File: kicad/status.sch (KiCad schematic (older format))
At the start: 34 parts, among them U28 74HC04, U29 74HC04

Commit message: bugfixed design
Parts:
- renumbered D30 to D52, D31 to D53, D32 to D54, D33 to D55, D34 to D56, D35 to D57, D36 to D58, D37 to D59, D38 to D60, D39 to D61, D40 to D62, D67 to D63, D41 to D64, D42 to D65, D43 to D66, D44 to D67, R7 to R24, R8 to R25, R9 to R26, R10 to R27, R11 to R28, R12 to R29, R13 to R30, R14 to R31, R15 to R32, R16 to R33, R17 to R34, R30 to R35, R18 to R36, R19 to R37, R20 to R38, R21 to R39, U28 to U45, U29 to U46

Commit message: design as built
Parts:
- renumbered D52 to D1101, D53 to D1102, D54 to D1103, D55 to D1104, D56 to D1105, D57 to D1106, D58 to D1107, D59 to D1108, D60 to D1109, D61 to D1110, D62 to D1111, D63 to D1112, D64 to D1113, D65 to D1114, D66 to D1115, D67 to D1116, R24 to R1101, R25 to R1102, R26 to R1103, R27 to R1104, R28 to R1105, R29 to R1106, R30 to R1107, R31 to R1108, R32 to R1109, R33 to R1110, R34 to R1111, R35 to R1112, R36 to R1113, R37 to R1114, R38 to R1115, R39 to R1116, U45 to U1101, U46 to U1102

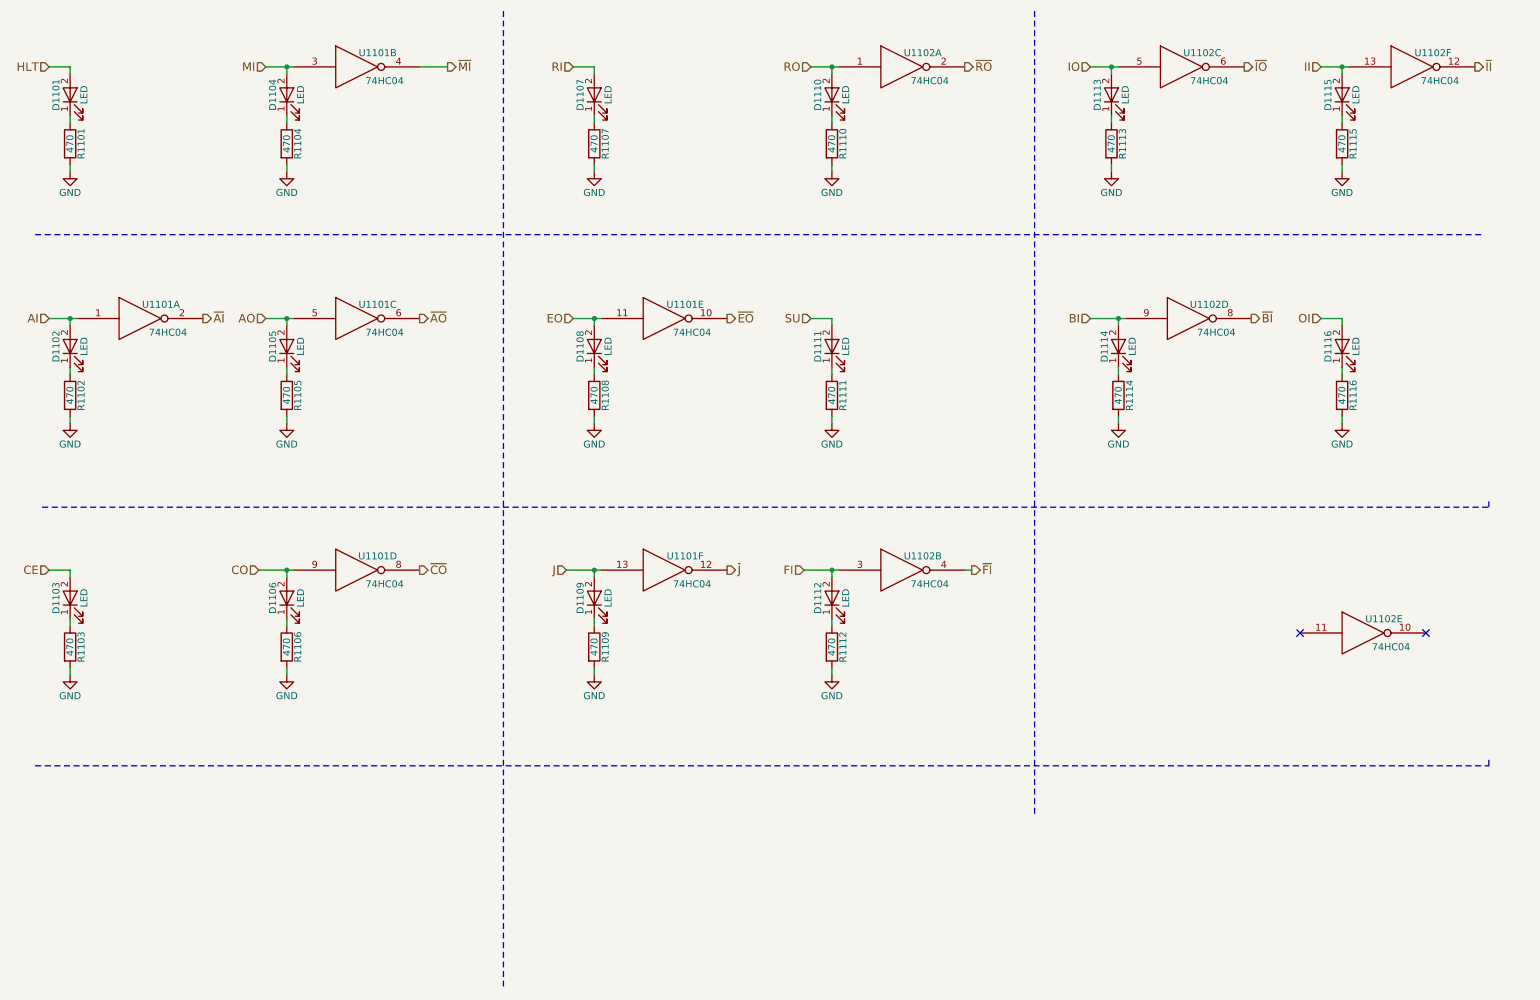
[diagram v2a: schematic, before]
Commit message: Update to current kicad version
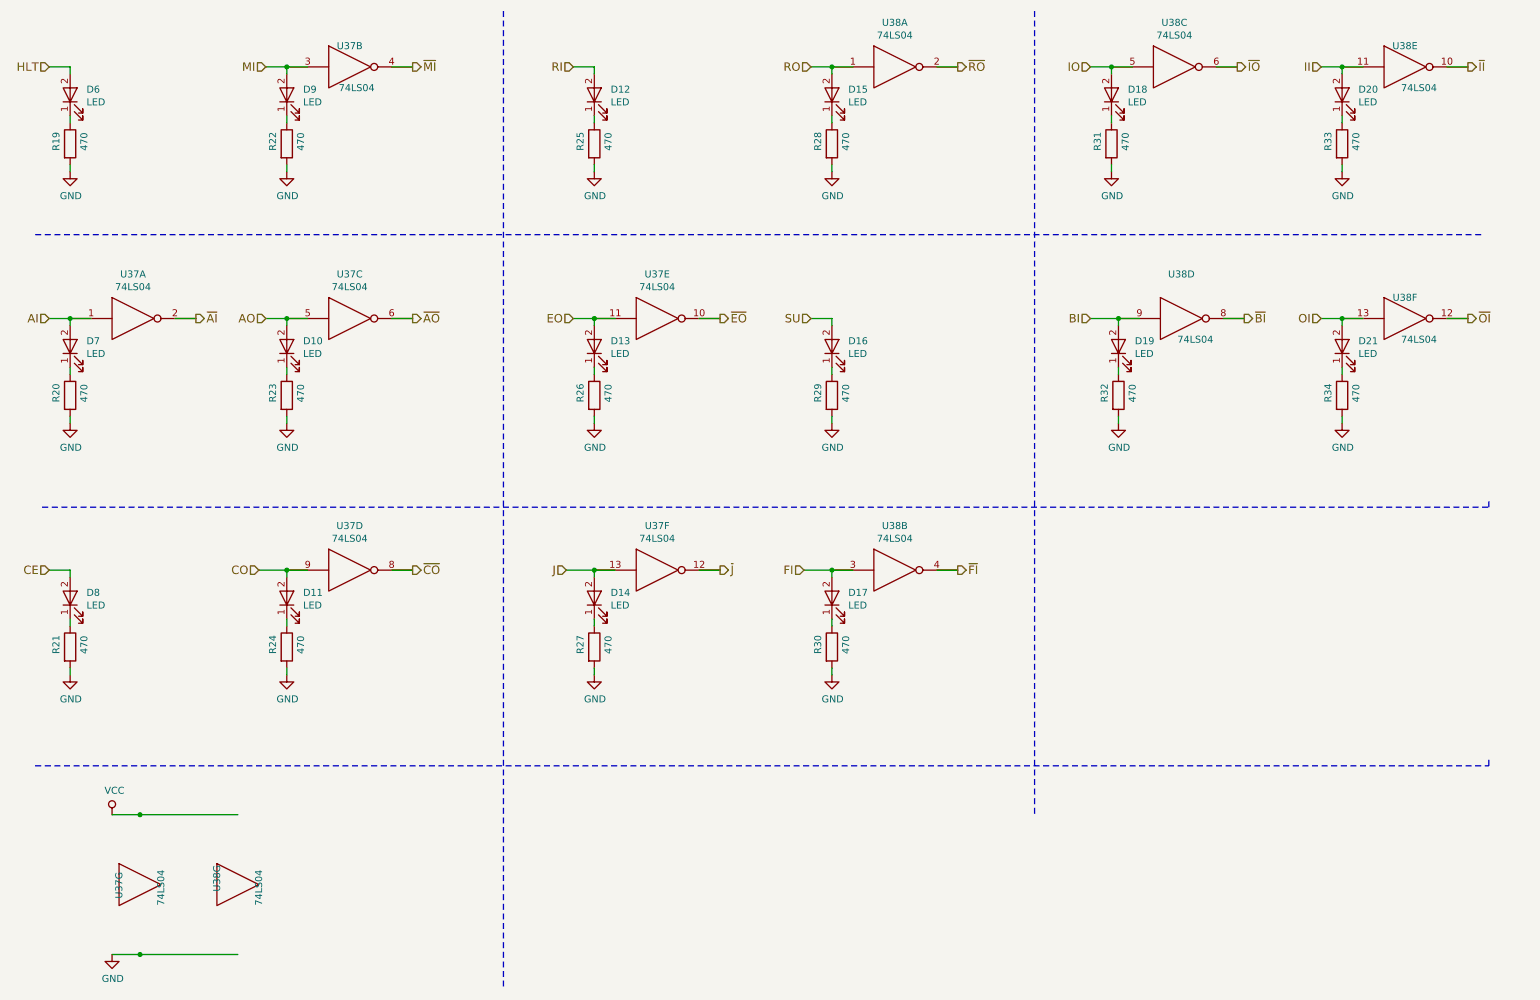
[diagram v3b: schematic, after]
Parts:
- removed D1101, D1102, D1103, D1104, D1105, D1106, D1107, D1108, D1109, D1110, D1111, D1112, D1113, D1114, D1115, D1116: LED, LEDs:LED-5MM, symbol LED
- removed R1101, R1102, R1103, R1104, R1105, R1106, R1107, R1108, R1109, R1110, R1111, R1112, R1113, R1114, R1115, R1116: 470, Resistors_THT:Resistor_Horizontal_RM7mm, symbol R
- removed U1101, U1102: 74HC04, Housings_DIP:DIP-14_W7.62mm_LongPads, symbol 74HC04
- added D10, D11, D12, D13, D14, D15, D16, D17, D18, D19, D20, D21, D6, D7, D8, D9: LED, symbol Device:LED
- added R19, R20, R21, R22, R23, R24, R25, R26, R27, R28, R29, R30, R31, R32, R33, R34: 470, symbol Device:R
- added U37, U38: 74LS04, symbol 74xx:74LS04
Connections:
- net labels added: VCC, ~OI
- wire segments 66 -> 92
- no-connect marks 2 -> 0
